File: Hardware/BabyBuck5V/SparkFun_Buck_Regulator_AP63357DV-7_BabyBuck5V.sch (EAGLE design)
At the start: 20 parts, among them U1 AP63357

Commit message: Renumbered parts to match other schematic.
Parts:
- C1: value 4.7uF -> 47pF; device SparkFun-Capacitors:4.7UF-0805-50V-(10%) -> SparkFun-Capacitors:47PF-0402_TIGHT-25V-5%-X7R
- C2: value 4.7uF -> 0.1uF; device SparkFun-Capacitors:4.7UF-0805-50V-(10%) -> SparkFun-Capacitors:0.1UF-0402T-16V-10%
- C3: value 0.1uF -> 22uF; device SparkFun-Capacitors:0.1UF-0402T-16V-10% -> SparkFun-Capacitors:22UF-0805-16V-20%
- C4: value 47pF -> 22uF; device SparkFun-Capacitors:47PF-0402_TIGHT-25V-5%-X7R -> SparkFun-Capacitors:22UF-0805-16V-20%
- C5, C6: value 22uF -> 4.7uF; device SparkFun-Capacitors:22UF-0805-16V-20% -> SparkFun-Capacitors:4.7UF-0805-50V-(10%)
- R1: value 93.1k -> 150k; device Buck5V:93.1KOHM-0402-1/16W-1%(93.1KOHM) -> SparkFun-Resistors:150KOHM-0402T-1/16W-1%; RES (none) -> 150k
- R2: value 22k -> 28.7k; device SparkFun-Resistors:22KOHM-0402_TIGHT-1/10W-1% -> Buck5V:28.7KOHM-0402-1/16W-1%(28.7KOHM)
- R3: value 150k -> 93.1k; device SparkFun-Resistors:150KOHM-0402T-1/16W-1% -> Buck5V:93.1KOHM-0402-1/16W-1%(93.1KOHM); RES 150k -> (none)
- R4: value 28.7k -> 22k; device Buck5V:28.7KOHM-0402-1/16W-1%(28.7KOHM) -> SparkFun-Resistors:22KOHM-0402_TIGHT-1/10W-1%
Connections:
- net 5V: now also C1.1, C3.1, R1.2; no longer C5.1, C6.1, R3.2
- net EN: now also R3.1, R4.2; no longer R1.1, R2.2
- net FB: now also C1.2, R1.1, R2.2; no longer C4.2, R3.1, R4.2
- net GND: now also C3.2, C4.2; no longer C1.2, C2.2
- net N$4: now also C2.1; no longer C3.1
- net SW: now also C2.2; no longer C3.2
- net VIN: now also C5.1, C6.1, R3.2; no longer C1.1, C2.1, R1.2
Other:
- moved on the sheet: C1, C2, C3, C4, C5, C6, R1, R2, R3, R4

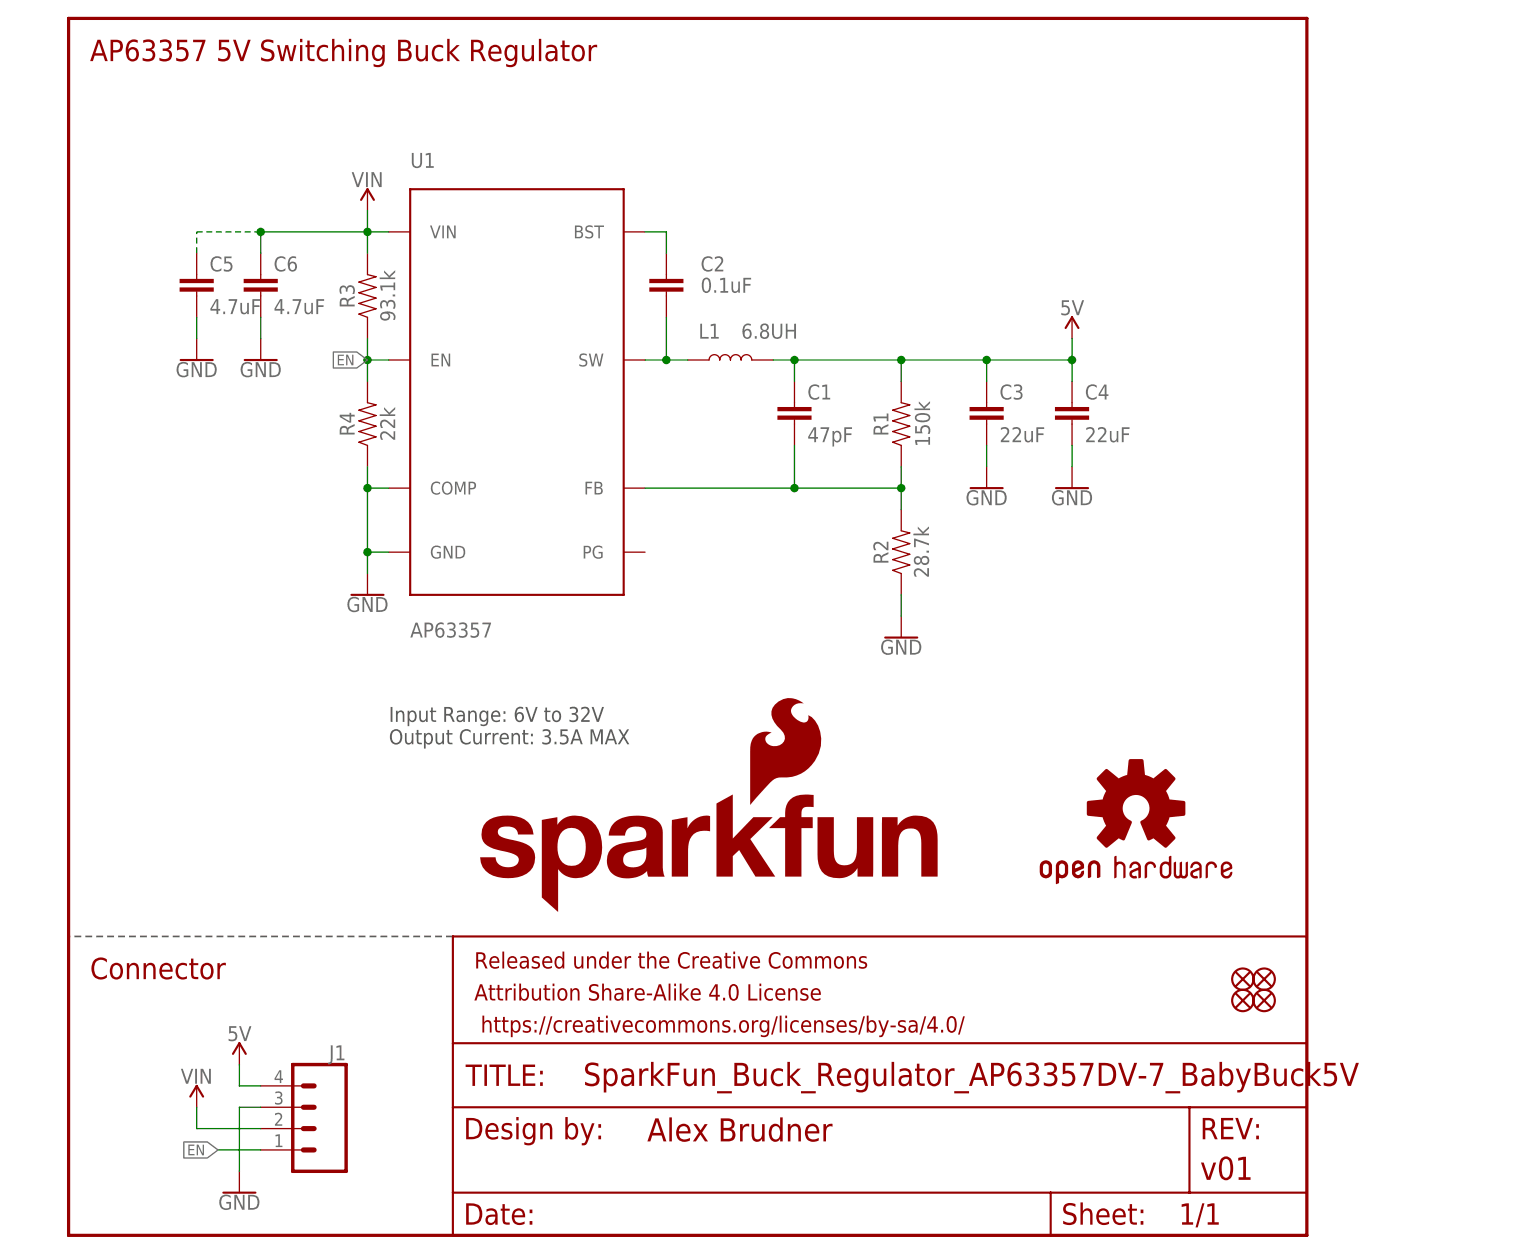
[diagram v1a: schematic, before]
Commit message: v01 changes implemented.
Schematic:
Add note for LED jumper
Add green wire for EN
Section titles center anchor
Rename Regulator section
Layout:
Increase selective solder width
Move 1x1 thermal pad
Make silk labels more explicit
Add "CAUTION: HOT" or just "HOT" silk
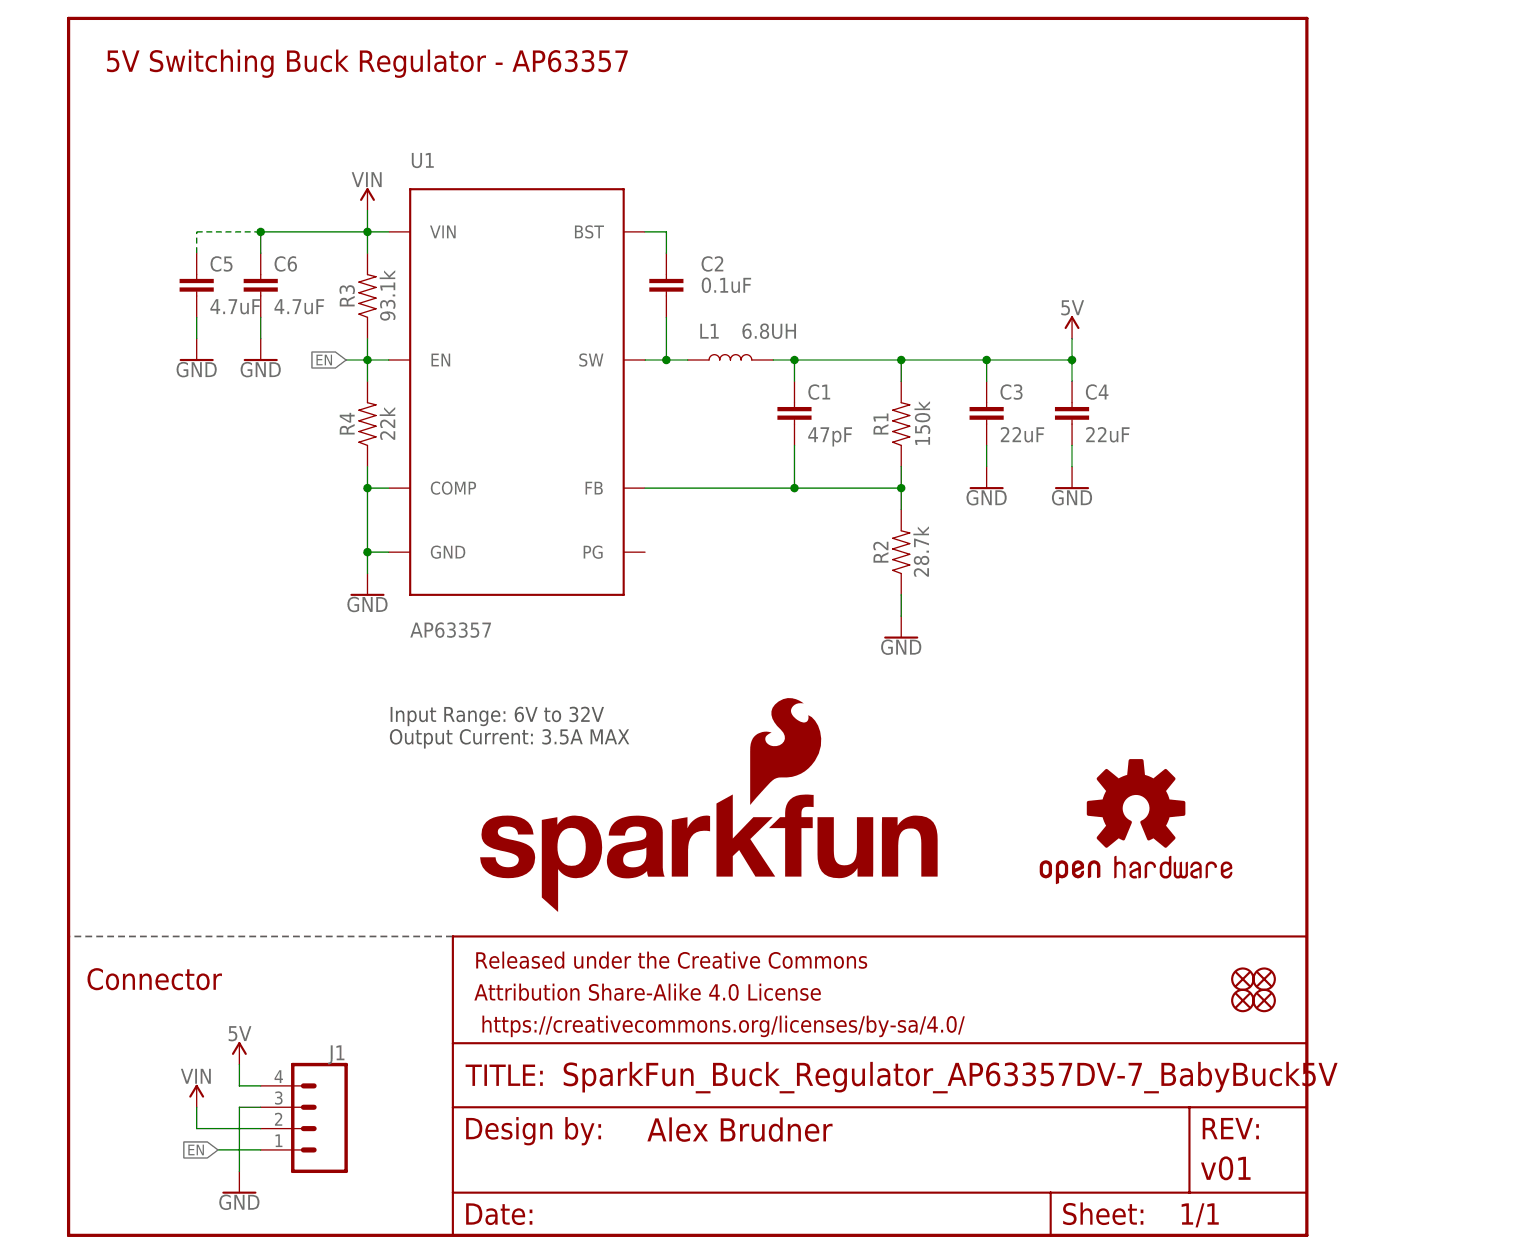
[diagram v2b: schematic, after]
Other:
- note added: "5V Switching Buck Regulator - AP63357"
- note removed: "AP63357 5V Switching Buck Regulator"
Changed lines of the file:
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@@
 <setting verticaltext="up"/>
 </settings>
-<grid distance="0.1" unitdist="inch" unit="inch" style="lines" multiple="1" display="no" altdistance="0.01" altunitdist="inch" altunit="inch"/>
+<grid distance="0.1" unitdist="inch" unit="inch" style="lines" multiple="1" display="yes" altdistance="0.01" altunitdist="inch" altunit="inch"/>
 <layers>
 <layer number="1" name="Top" color="4" fill="1" visible="no" active="no"/>
@@
 <wire x1="147.32" y1="144.78" x2="0" y2="144.78" width="0.381" layer="94"/>
 <wire x1="0" y1="144.78" x2="0" y2="0" width="0.381" layer="94"/>
-<text x="2.54" y="139.7" size="2.54" layer="94" font="vector">AP63357 5V Switching Buck Regulator</text>
+<text x="35.56" y="139.7" size="2.54" layer="94" font="vector" align="center">5V Switching Buck Regulator - AP63357</text>
 <text x="38.1" y="58.42" size="1.778" layer="97" font="vector">Input Range: 6V to 32V
 Output Current: 3.5A MAX</text>
-<text x="2.54" y="30.48" size="2.54" layer="94" font="vector">Connector</text>
+<text x="10.16" y="30.48" size="2.54" layer="94" font="vector" align="center">Connector</text>
 <wire x1="45.72" y1="35.56" x2="0" y2="35.56" width="0.2032" layer="97" style="longdash"/>
 </plain>
@@
 <attribute name="LAST_DATE_TIME" x="58.42" y="1.27" size="2.54" layer="94" font="vector"/>
 <attribute name="SHEET" x="132.08" y="1.27" size="2.54" layer="94" font="vector"/>
-<attribute name="DRAWING_NAME" x="61.214" y="17.78" size="2.7432" layer="94" font="vector"/>
+<attribute name="DRAWING_NAME" x="58.674" y="17.78" size="2.7432" layer="94" font="vector"/>
 <attribute name="DESIGNER" x="68.834" y="11.176" size="2.7432" layer="94" font="vector"/>
 <attribute name="REV" x="134.62" y="6.604" size="2.7432" layer="94" font="vector"/>
@@
 <wire x1="35.56" y1="101.6" x2="35.56" y2="104.14" width="0.1524" layer="91"/>
 <junction x="35.56" y="104.14"/>
-<label x="35.56" y="104.14" size="1.27" layer="95" rot="R180" xref="yes"/>
-</segment>
-<segment>
+<label x="33.02" y="104.14" size="1.27" layer="95" rot="R180" xref="yes"/>
+<wire x1="35.56" y1="104.14" x2="33.02" y2="104.14" width="0.1524" layer="91"/>
+</segment>
+<segment>

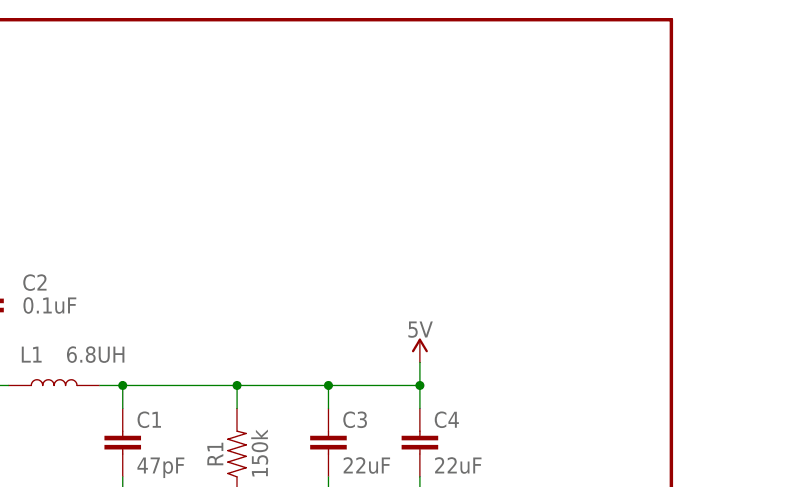
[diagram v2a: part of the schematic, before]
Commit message: Added gerbers for v01, added UVLO text to babybuck sch.
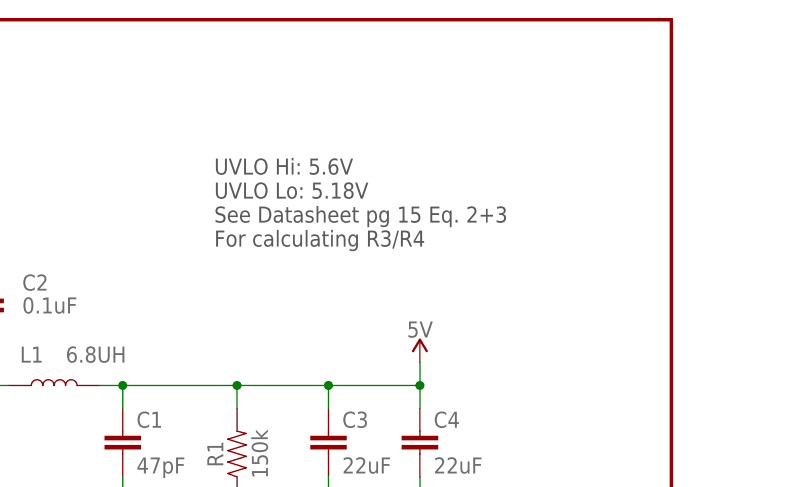
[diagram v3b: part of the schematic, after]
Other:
- note added: "UVLO Hi: 5.6V UVLO Lo: 5.18V See Datasheet pg 15 Eq. 2+3 For calculating R3/R4"
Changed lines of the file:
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@@
 <text x="10.16" y="30.48" size="2.54" layer="94" font="vector" align="center">Connector</text>
 <wire x1="45.72" y1="35.56" x2="0" y2="35.56" width="0.2032" layer="97" style="longdash"/>
+<text x="96.52" y="124.46" size="1.778" layer="97" font="vector" align="center-left">UVLO Hi: 5.6V
+UVLO Lo: 5.18V
+See Datasheet pg 15 Eq. 2+3
+For calculating R3/R4</text>
 </plain>
 <instances>
